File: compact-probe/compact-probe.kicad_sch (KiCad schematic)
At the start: 26 parts, among them IC1 ATA6561-GBQW-N, J1 Conn_01x08_Male, J2 Conn_01x04_Male, J3 Conn_02x05_Odd_Even, J4 Conn_01x01_Female, J5 Conn_01x01_Female, J6 Conn_01x01_Female, J7 Conn_01x01_Female, J8 Conn_01x01_Female, U4 ESP32-C3-WROOM-02-H4, U6 LT1963AxST-3.3

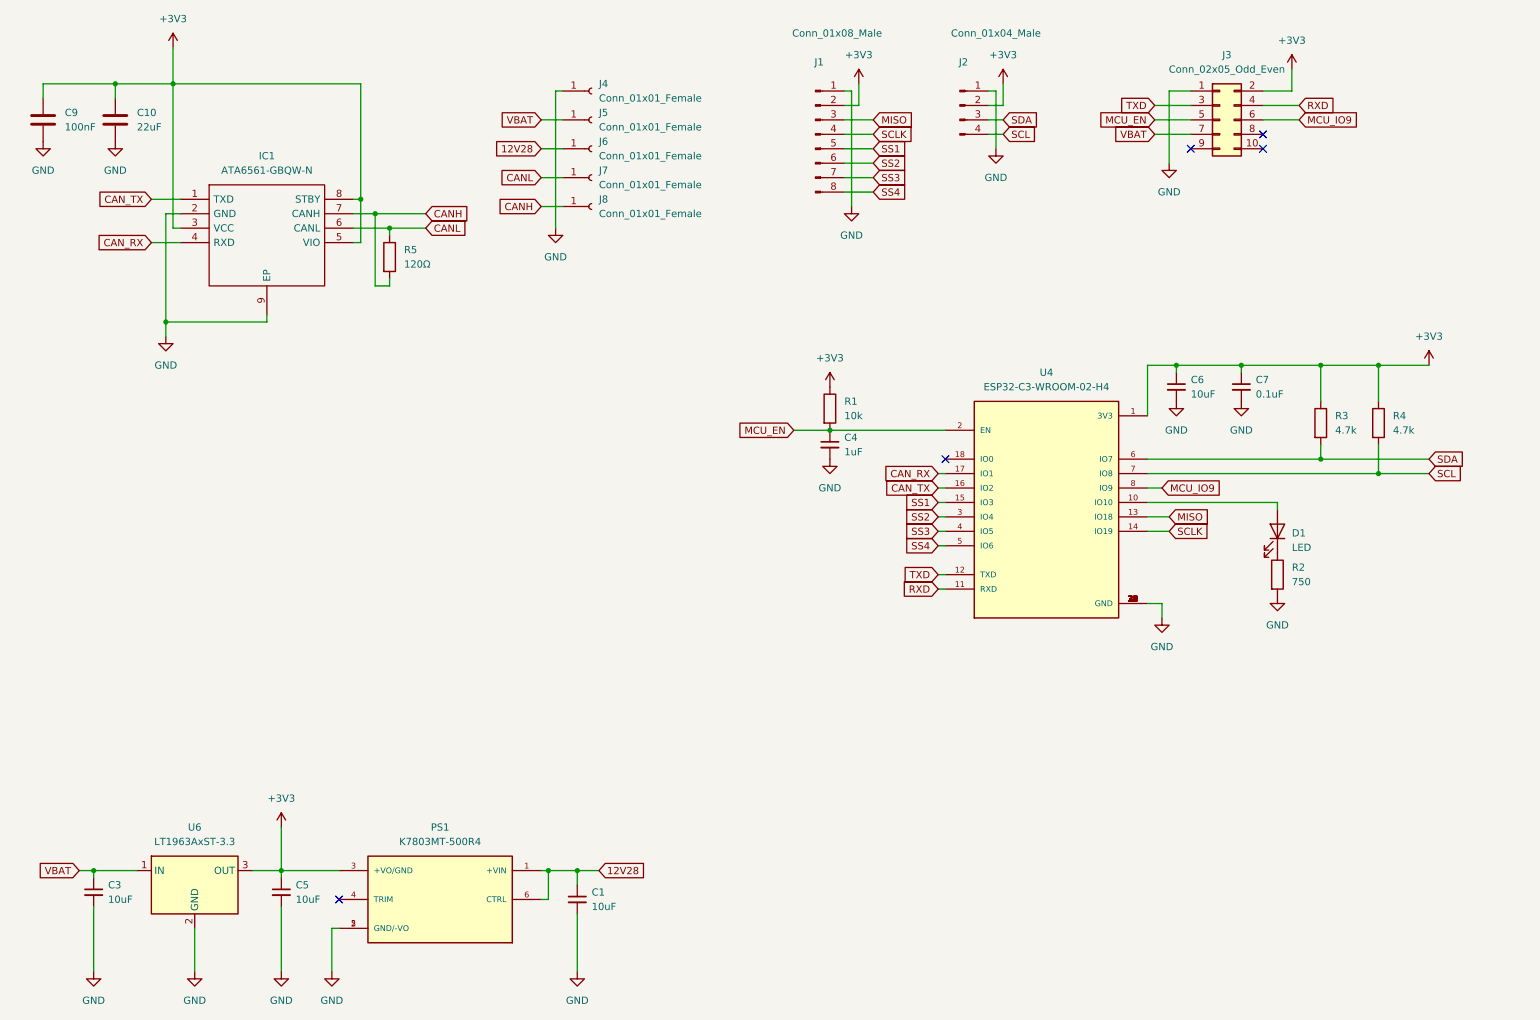
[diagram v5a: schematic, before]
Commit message: Changed to new power supply and different CANBus chip.
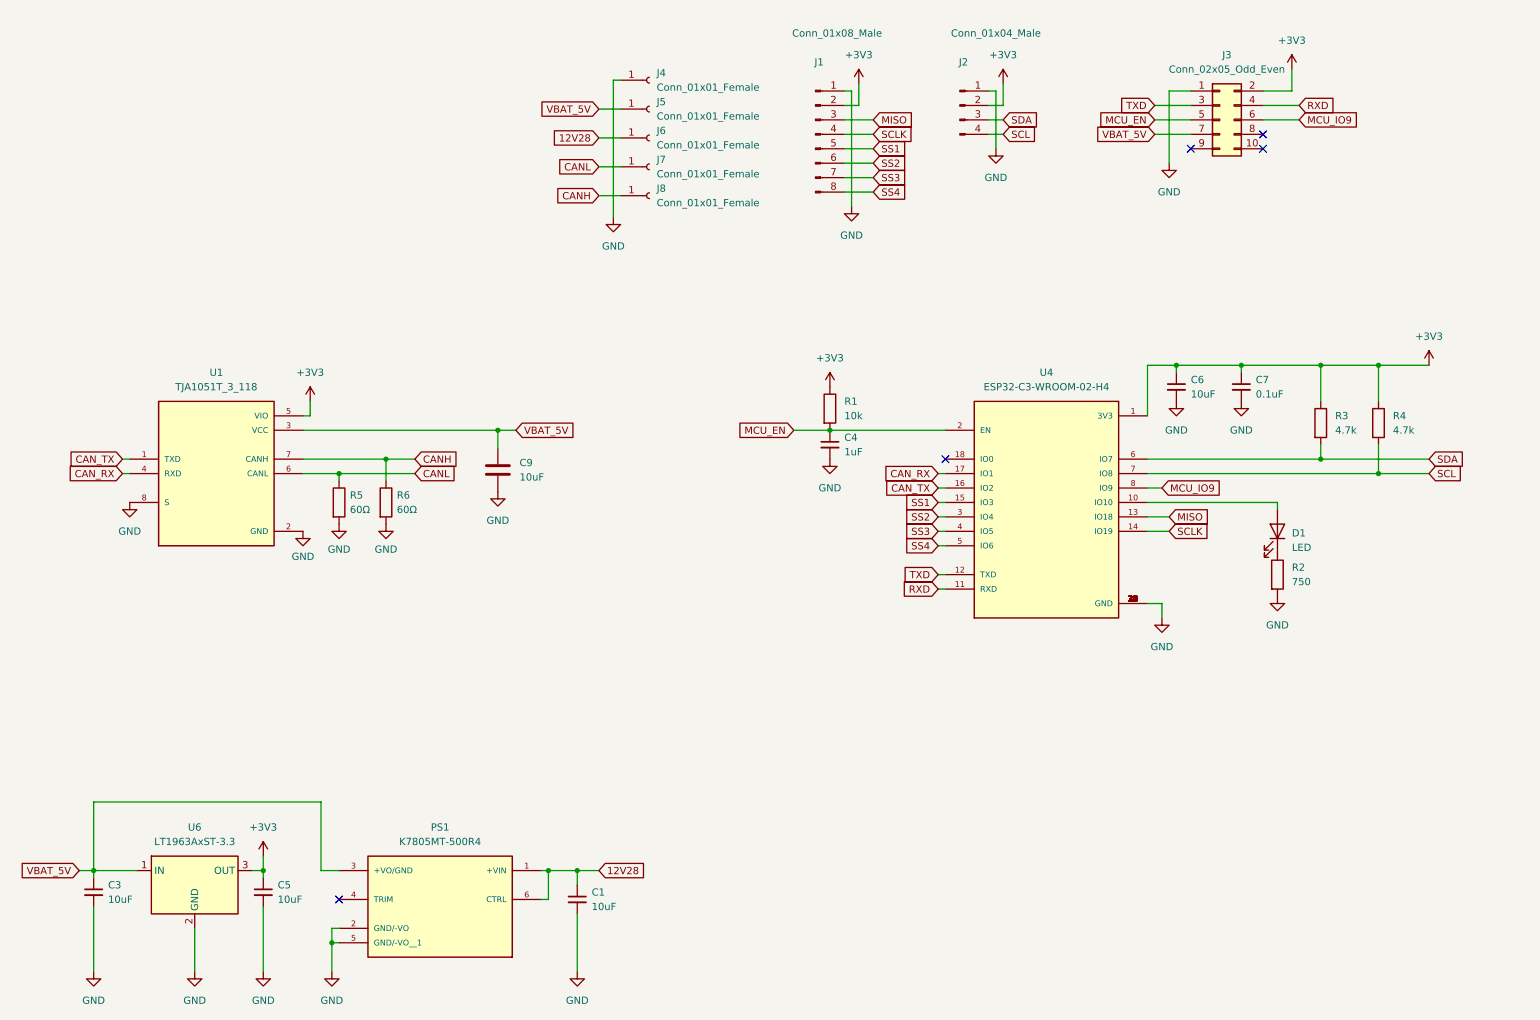
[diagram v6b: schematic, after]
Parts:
- removed C10: 22uF, Capacitor_SMD:C_0603_1608Metric, symbol Device:C
- removed IC1: ATA6561-GBQW-N, airball-hardware:SON65P300X300X90-9N-D, symbol airball-hardware:ATA6561-GBQW-N
- removed PS1: K7803MT-500R4, airball-hardware:CONV_K7803MT-500R4, symbol airball-hardware:K7803MT-500R4
- added PS1: K7805MT-500R4, airball-hardware:CONV_K7805MT-500R4, symbol airball-hardware:K7805MT-500R4
- added R6: 60Ω, Resistor_SMD:R_0603_1608Metric, symbol Device:R
- added U1: TJA1051T_3_118, airball-hardware:TJA1051T_3_118, symbol airball-hardware:TJA1051T_3_118
- C9: value 100nF -> 10uF
- R5: value 120Ω -> 60Ω
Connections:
- net +3V3: now also U1.5 (VIO); no longer C9.1
- net 12V28: now also PS1.1 (+VIN), PS1.6 (CTRL)
- net CANH: now also R6.1, U1.7 (CANH); no longer R5.2
- net CANL: now also U1.6 (CANL)
- net CAN_RX: now also U1.4 (RXD)
- net CAN_TX: now also U1.1 (TXD)
- net GND: now also R5.2, PS1.2 (GND/-VO), PS1.5 (GND/-VO__1), R6.2, U1.2 (GND), U1.8 (S)
- net VBAT renamed VBAT_5V
- net VBAT_5V: now also C9.1, PS1.3 (+VO/GND), U1.3 (VCC)
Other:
- moved on the sheet: C5, C9, J4, J5, J6, J7, J8, R5
